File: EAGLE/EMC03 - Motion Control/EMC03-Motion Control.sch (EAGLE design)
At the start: 37 parts, among them J1 HR911105A, Q2 25MHz, U1 LPC1768LQFP-100, U3 CPL-ETH-PHY-LAN8720A, U4 74LVC1G04

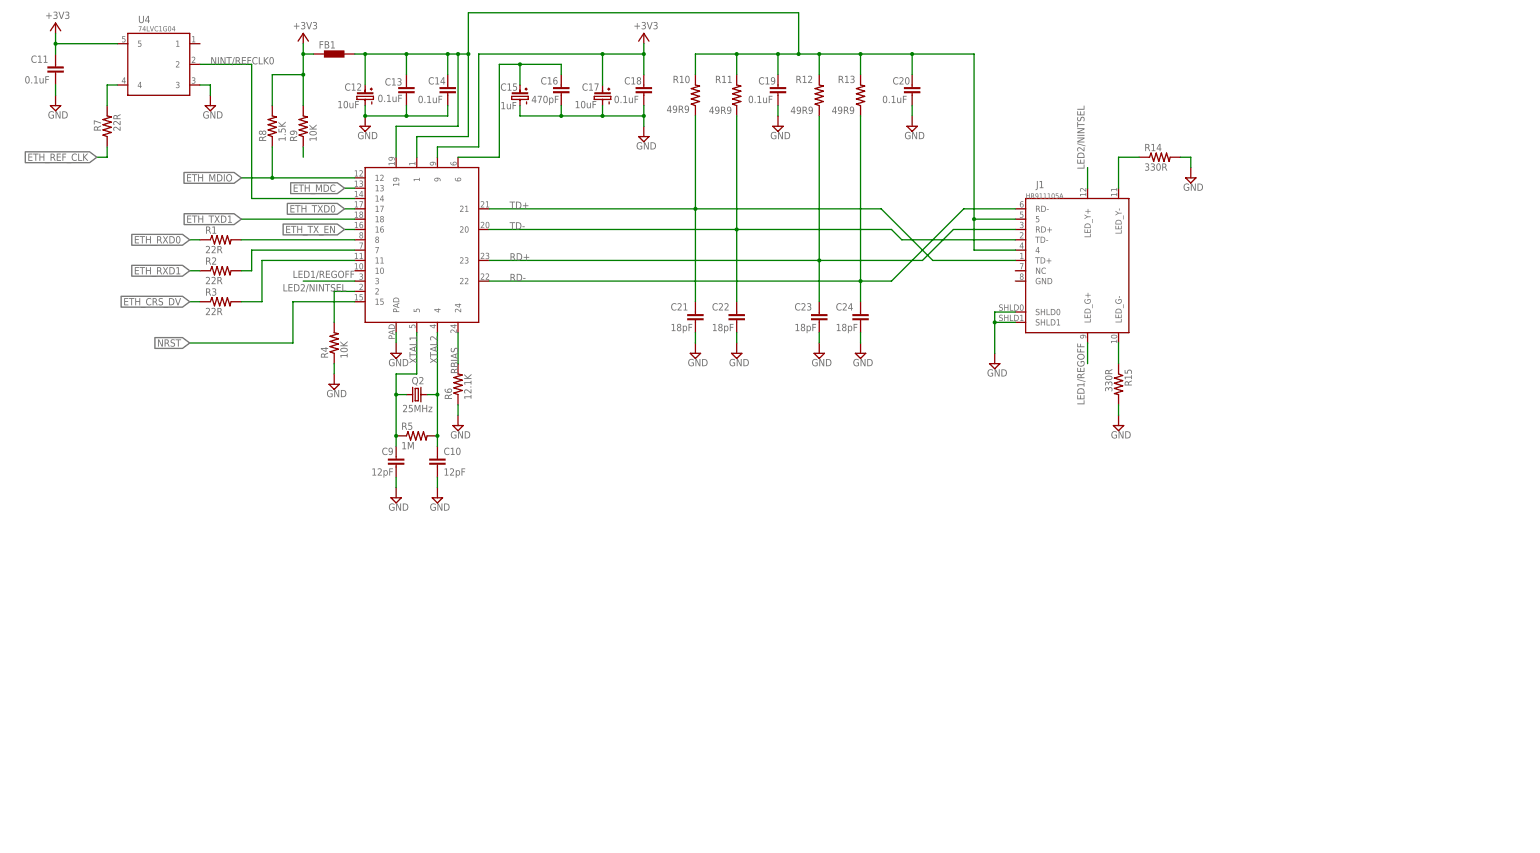
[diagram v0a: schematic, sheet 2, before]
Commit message: Added parts for USB, MicroSD, and SWD connections, imported all into schematic for EMC03 board, named and labeled all relevant connections.
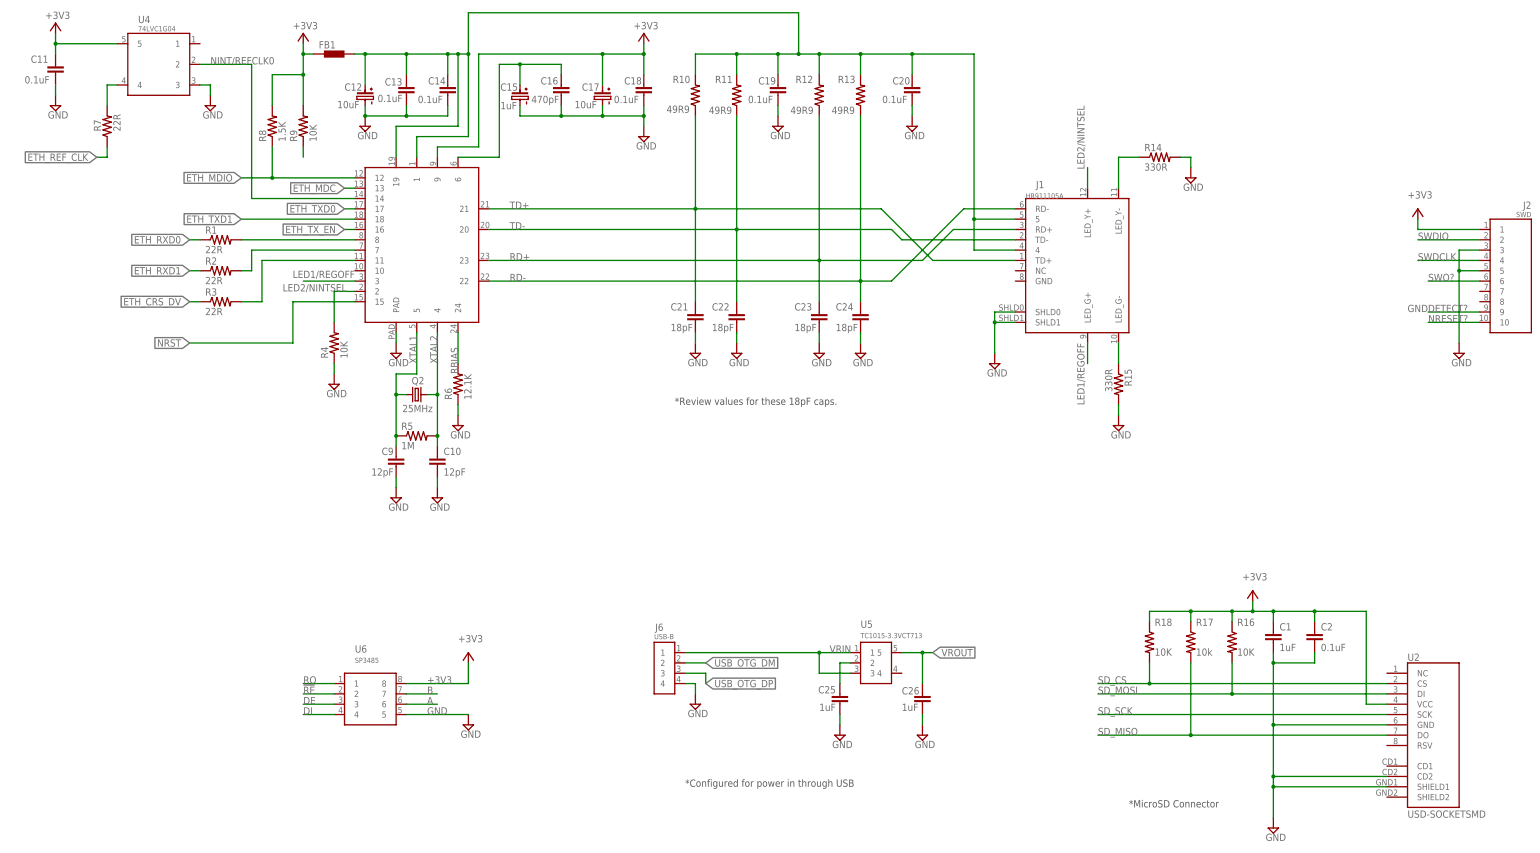
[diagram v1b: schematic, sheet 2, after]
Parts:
- added C1, C25, C26: 1uF, TinWhiskers:CPL-CAP-X5R-0603-1UF-50V
- added C2: 0.1uF, TinWhiskers:CPL-CAP-X5R-0603-0.1UF-35V
- added J2: SWD, TinWhiskers:CPL-CON-HEADER-0.05IN-10P-M
- added J6: USB-B, TinWhiskers:CPL-CON-USB-B
- added R16, R18: 10K, TinWhiskers:CPL-RES-0603-10K-0.1W
- added R17: 10k, TinWhiskers:CPL-RES-0603-10K-0.1W
- added U2: USD-SOCKETSMD, TinWhiskers:USD-SOCKETSMD
- added U5: TC1015-3.3VCT713, TinWhiskers:CPL-REG-LIN-3.3V-0.1A
- added U6: SP3485, TinWhiskers:SP3485
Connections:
- new net !RE: U6.2
- new net A: U6.6
- new net B: U6.7
- new net DE: U6.3
- new net DI: U6.4
- new net GNDDETECT?: J2.9
- new net N$17: C25.2, U5.2
- new net NRESET?: J2.10
- new net RO: U6.1
- new net SD_CS: R18.2, U2.CS
- new net SD_MISO: R17.2, U2.DO
- new net SD_MOSI: R16.2, U2.DI
- new net SD_SCK: U2.SCK
- new net SWDCLK: J2.4
- new net SWDIO: J2.2
- new net SWO?: J2.6
- new net USB_OTG_DM: J6.2
- new net USB_OTG_DP: J6.3
- new net VRIN: J6.1, U5.1, U5.3
- new net VROUT: C26.2, U5.5
- net +3V3: now also C1.2, C2.2, J2.1, R16.1, R17.1, R18.1, U2.VCC, U6.8
- net GND: now also C1.1, C2.1, C25.1, C26.1, J2.3, J2.5, J6.4, U2.CD2, U2.GND, U2.SHIELD1, U6.5
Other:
- note added: "*Configured for power in through USB"
- note added: "*MicroSD Connector"
- note added: "*Review values for these 18pF caps."

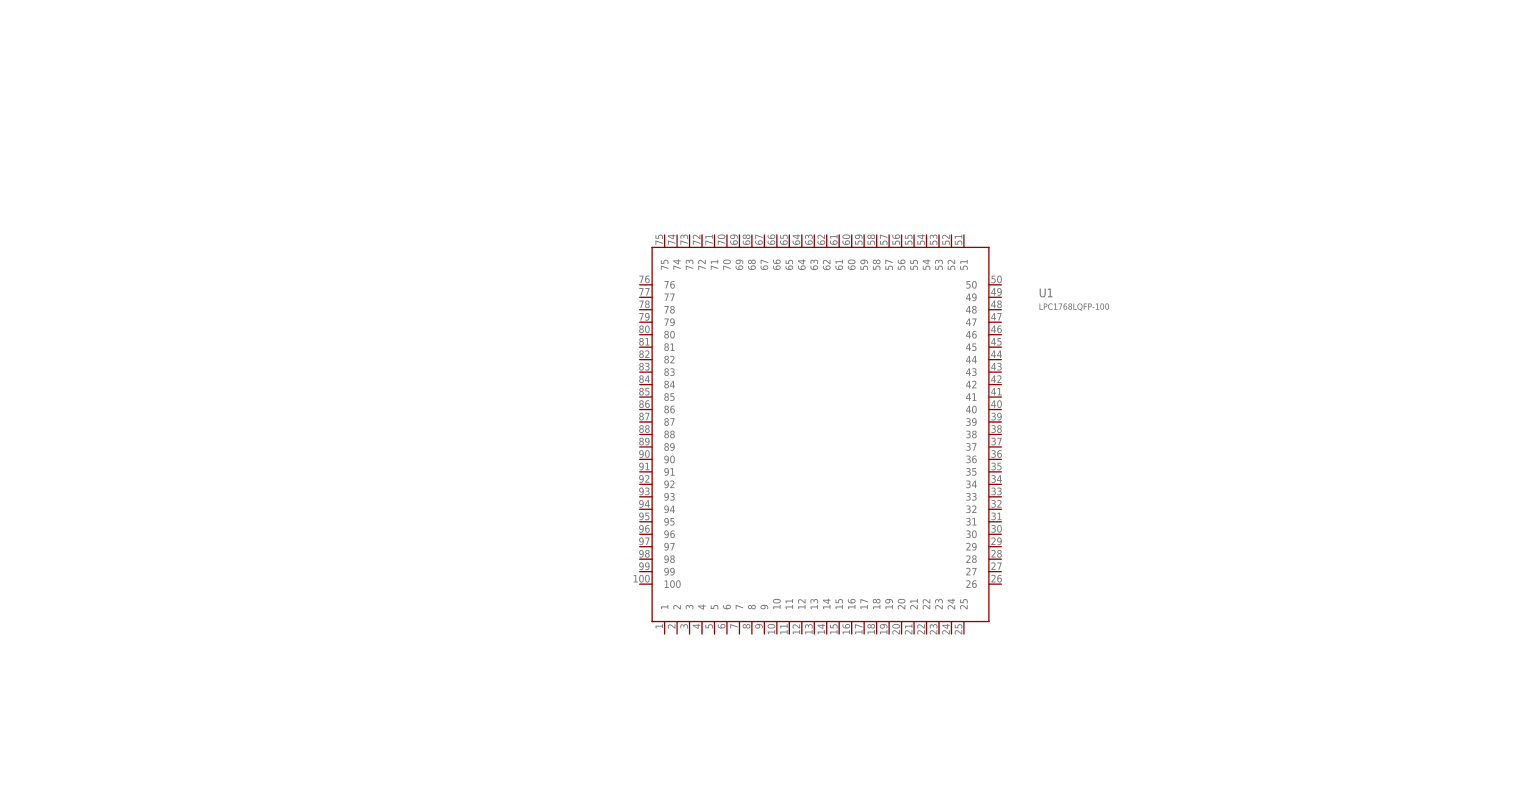
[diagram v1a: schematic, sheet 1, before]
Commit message: Added RS-485 chip, connected ethernet, SD, USB to processor. Connected power net to processor.
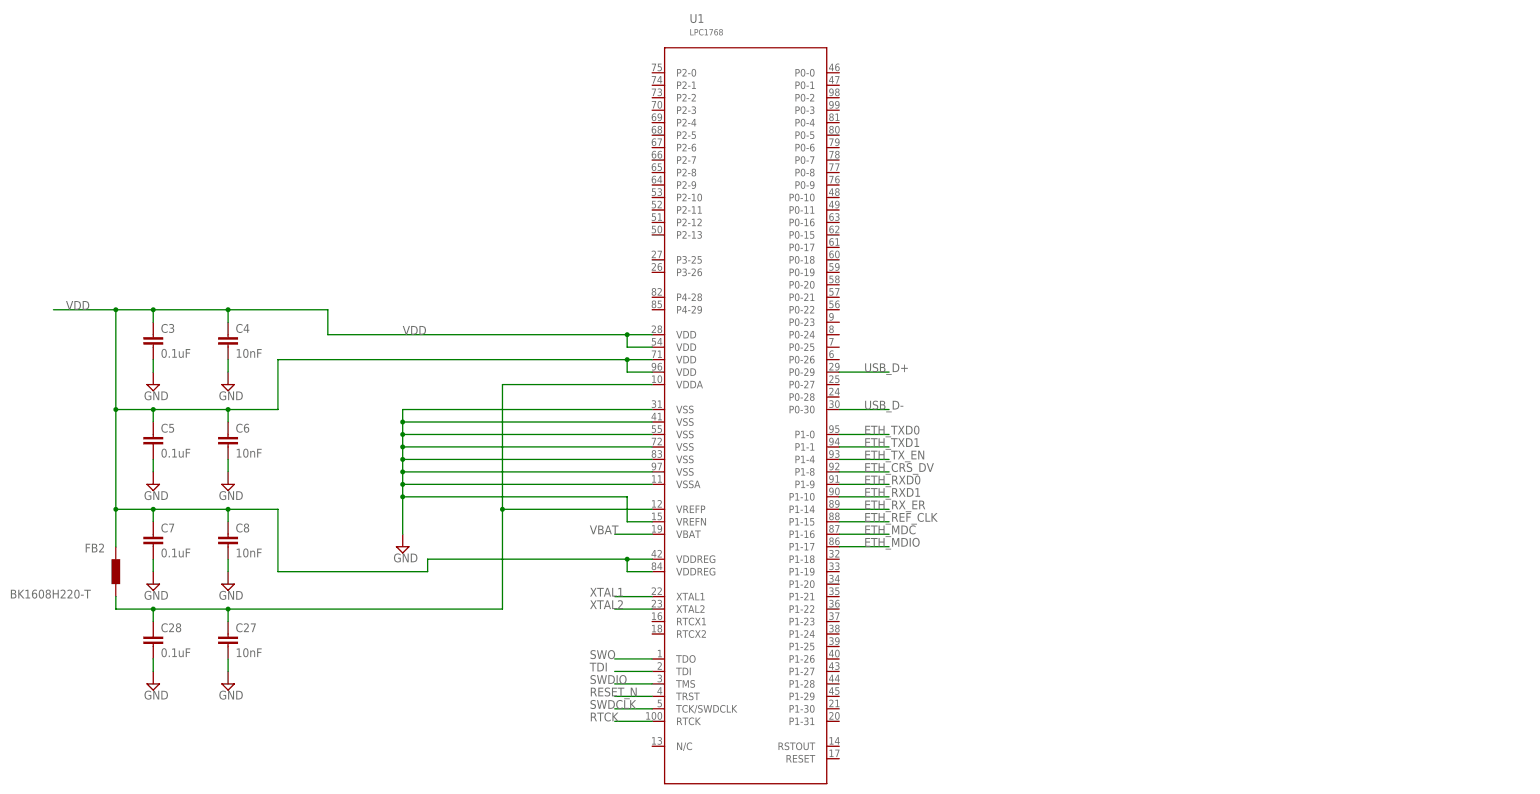
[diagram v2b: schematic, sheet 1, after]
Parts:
- added C27, C4, C6, C8: 10nF, TinWhiskers:CPL-CAP-X7R-10NF-16V
- added C28, C3, C5, C7: 0.1uF, TinWhiskers:CPL-CAP-X5R-0603-0.1UF-35V
- added FB2: BK1608H220-T, TinWhiskers:BLM15HBK1608H220-T0603
- FB1: value BLM15H0603 -> BLM15HBK1608H220-T0603; device TinWhiskers:BLM15H0603 -> TinWhiskers:BLM15HBK1608H220-T0603
- U1: value LPC1768LQFP-100 -> LPC1768
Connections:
- removed net GNDDETECT?: J2.9
- removed net NRESET?: J2.10
- removed net SWO?: J2.6
- removed net USB_OTG_DM: J6.2
- removed net USB_OTG_DP: J6.3
- new net GND1: C27.1
- new net N$2: C27.2, C28.2, FB2.1, U1.VDDA, U1.VREFP
- new net RESET_N: J2.10, U1.TRST
- new net RTCK: J2.7, U1.RTCK
- new net SWO: J2.6, U1.TDO
- new net TDI: J2.8, U1.TDI
- new net USB_D+: J6.3, U1.P0-29
- new net USB_D-: J6.2, U1.P0-30
- new net VBAT: U1.VBAT
- new net VDD: C3.2, C4.2, C5.2, C6.2, C7.2, C8.2, FB2.2, U1.VDD@28, U1.VDD@54, U1.VDD@71, U1.VDD@96, U1.VDDREG@42, U1.VDDREG@84
- net ETH_CRS_DV: now also U1.P1-8
- net ETH_MDC: now also U1.P1-16
- net ETH_MDIO: now also U1.P1-17
- net ETH_REF_CLK: now also U1.P1-15
- net ETH_RXD0: now also U1.P1-9
- net ETH_RXD1: now also U1.P1-10
- net ETH_RX_ER: now also U1.P1-14, U3.10
- net ETH_TXD0: now also U1.P1-0
- net ETH_TXD1: now also U1.P1-1
- net ETH_TX_EN: now also U1.P1-4
- net GND: now also C28.1, C3.1, C4.1, C5.1, C6.1, C7.1, C8.1, J2.9, U1.VREFN, U1.VSS@31, U1.VSS@41, U1.VSS@55, U1.VSS@72, U1.VSS@83, U1.VSS@97, U1.VSSA
- net SWDCLK: now also U1.TCK/SWDCLK
- net SWDIO: now also U1.TMS
- net XTAL1: now also U1.XTAL1
- net XTAL2: now also U1.XTAL2
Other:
- moved on the sheet: R7, U1, U4

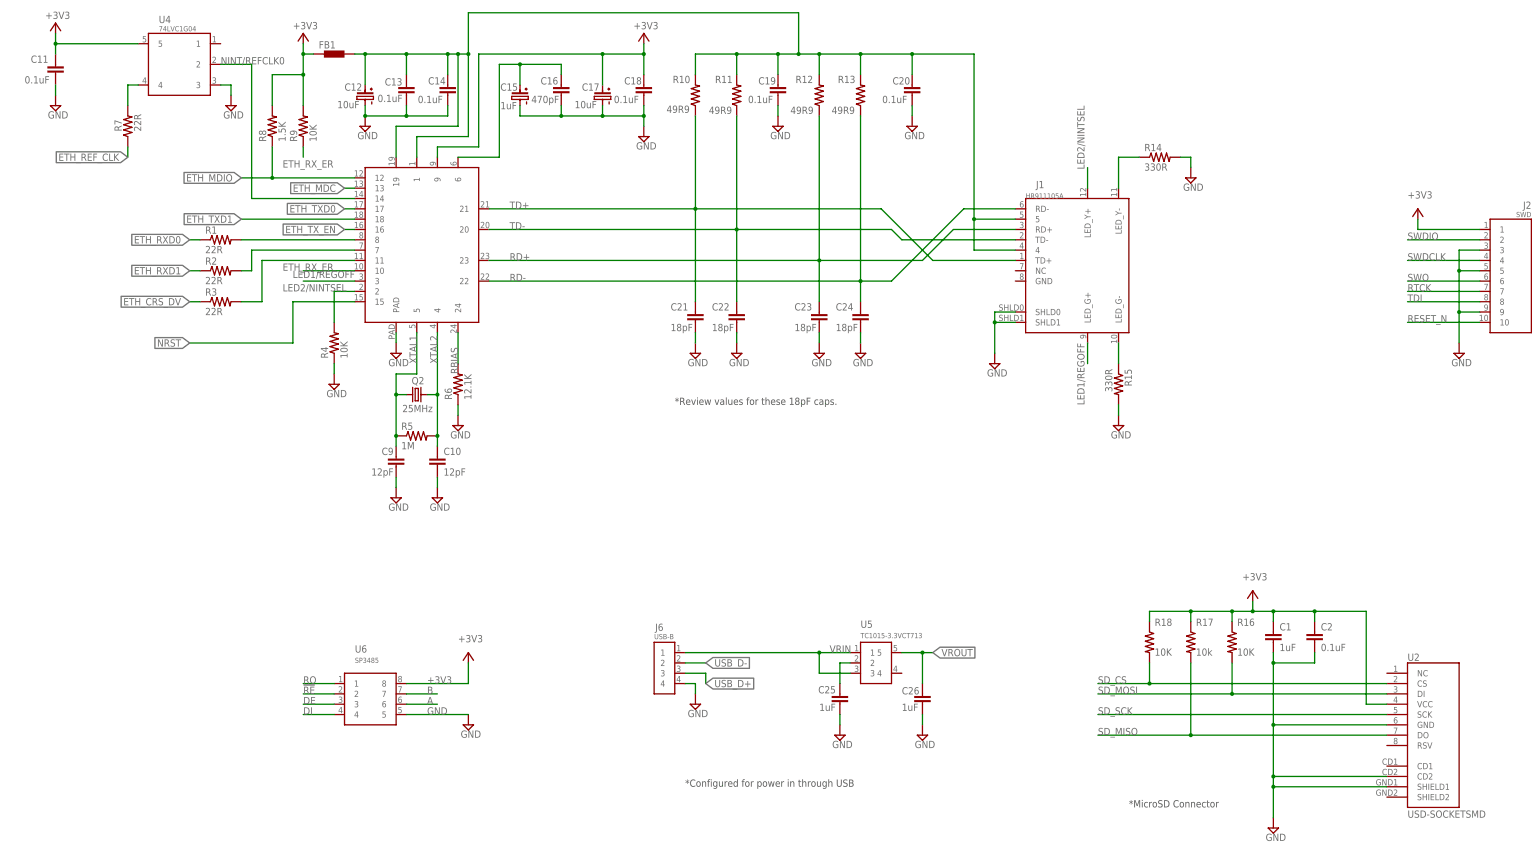
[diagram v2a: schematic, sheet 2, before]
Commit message: Updated schematic to include UART0, UART1, MicroSD, SWD, RS-485.
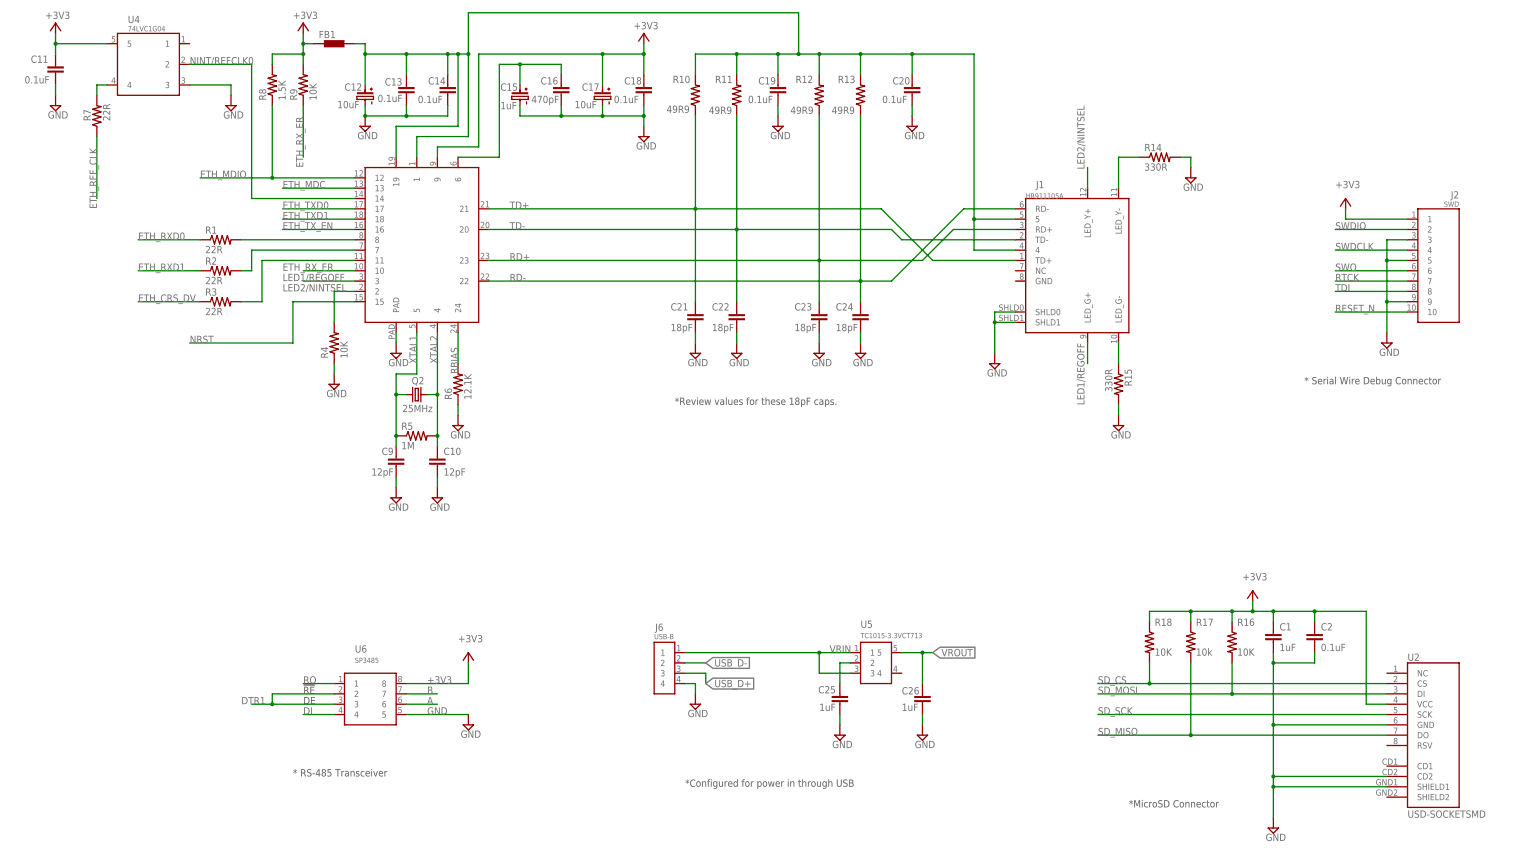
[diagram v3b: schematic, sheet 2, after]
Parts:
- added C29: 0.1uF, TinWhiskers:CPL-CAP-X7R-0603-0.1UF-35V
- added J3: UART0, TinWhiskers:CPL-CON-HEADER-0.1IN-6P-M
- added R19: 10k, TinWhiskers:CPL-RES-0603-10K-0.1W
- added S1: SWS001, smd-special:SWS001
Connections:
- removed net !RE: U6.2
- removed net DE: U6.3
- new net DTR: C29.1, J3.6
- new net DTR1: U1.P0-20, U6.2, U6.3
- new net RESET: C29.2, R19.1, S1.2, U1.RESET
- new net RXI: J3.5
- new net TXO: J3.4
- net +3V3: now also J3.3, R19.2
- net DI: now also U1.P0-15
- net GND: now also J3.1, J3.2, S1.1
- net RO: now also U1.P0-16
- net SD_CS: now also U1.P0-6
- net SD_MISO: now also U1.P0-8
- net SD_MOSI: now also U1.P0-9
- net SD_SCK: now also U1.P0-7
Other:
- note added: "!RE"
- note added: "* RS-485 Transceiver"
- note added: "* Serial Wire Debug Connector"
- note added: "DE"
- note added: "VDD"
- moved on the sheet: FB1, J2, R7, R8, R9, U4
